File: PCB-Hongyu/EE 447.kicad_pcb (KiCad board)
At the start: 4 copper layers, 57.4 x 100 mm, 78 parts, among them J10 84952-4, J2 FH34SRJ-24S-0.5SH_99_, J3 S2B-PH-K-SLFSN, J4 Conn_01x01_Pin, J5 Conn_01x02_Pin, J6 Conn_01x01_Pin, J7 Conn_01x01_Pin, J8 Conn_01x02_Pin, J9 61302421121, Q1 BSS138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

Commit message: sdfghjk
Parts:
- Q2: footprint Package_TO_SOT_THT:TO-92_Inline -> Package_TO_SOT_SMD:SOT-23_Handsoldering
- moved Q2 2.80 mm to (206.5, 126.0)
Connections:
- J10 pad 5: GND -> (no net)
- J10 pad 6: GND -> (no net)
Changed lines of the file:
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@@
 			(psa4output no)
 			(plot_black_and_white yes)
+			(plotinvisibletext no)
 			(sketchpadsonfab no)
 			(plotpadnumbers no)
@@
 			)
 		)
-		(property "Datasheet" "https://www.digikey.com/en/products/detail/onsemi/BSS138/244210"
+		(property "Datasheet" "https://www.mouser.com/ProductDetail/onsemi-Fairchild/BSS138?qs=HK%252BeIG1iaahCeqBvjB4arg%3D%3D&srsltid=AfmBOoqSNHRxNY05tuDQ32Q_ya6yO_gO9lrnV_3A-Ol45sM-SCPd4I5t"
 			(at 0 0 0)
 			(layer "F.Fab")
@@
 			(size 2.667 3.6068)
 			(layers "F.Cu" "F.Mask" "F.Paste")
-			(net 1 "GND")
 		)
 		(pad "6" smd rect
@@
 			(size 2.667 3.6068)
 			(layers "F.Cu" "F.Mask" "F.Paste")
-			(net 1 "GND")
 		)
 		(embedded_fonts no)
@@
 		)
 	)
-	(footprint "Package_TO_SOT_THT:TO-92_Inline"
+	(footprint "Package_TO_SOT_SMD:SOT-23_Handsoldering"
 		(layer "F.Cu")
-		(at 209 127.27 90)
-		(descr "TO-92 leads in-line, narrow, oval pads, drill 0.75mm (see NXP sot054_po.pdf)")
-		(tags "to-92 sc-43 sc-43a sot54 PA33 transistor")
+		(at 206.5 126 90)
+		(descr "SOT-23, Handsoldering")
+		(tags "SOT-23")
 		(property "Reference" "Q2"
-			(at 1.27 -3.56 90)
+			(at 0 -2.75 90)
 			(layer "F.SilkS")
 			(effects
@@
 		)
 		(property "Value" "S8050"
-			(at 1.27 2.79 90)
+			(at 0 2.5 90)
 			(layer "F.Fab")
 			(effects
@@
 		(sheetname "/Epaper/")
 		(sheetfile "../PCB_June/PCB.kicad_sch")
-		(attr through_hole)
+		(attr smd)
 		(fp_line
-			(start -0.53 1.85)
-			(end 3.07 1.85)
+			(start 0.76 -1.58)
+			(end 0.76 -0.65)
 			(stroke
 				(width 0.12)
@@
 			(layer "F.SilkS")
 		)
-		(fp_arc
-			(start 1.27 -2.6)
-			(mid 3.672087 -0.994977)
-			(end 3.108478 1.838478)
+		(fp_line
+			(start -0.04 -1.58)
+			(end 0.76 -1.58)
 			(stroke
 				(width 0.12)
@@
 			(layer "F.SilkS")
 		)
-		(fp_arc
-			(start -0.568478 1.838478)
-			(mid -1.132087 -0.994977)
-			(end 1.27 -2.6)
+		(fp_line
+			(start -0.04 -1.58)
+			(end -0.84 -1.58)
+			(stroke
+				(width 0.12)
+				(type solid)
+			)
+			(layer "F.SilkS")
+		)
+		(fp_line
+			(start 0.76 1.58)
+			(end 0.76 0.65)
+			(stroke
+				(width 0.12)
+				(type solid)
+			)
+			(layer "F.SilkS")
+		)
+		(fp_line
+			(start 0.76 1.58)
+			(end -0.7 1.58)
 			(stroke
 				(width 0.12)
@@
 			(layer "F.SilkS")
 		)
+		(fp_poly
+			(pts
+				(xy -1.34 -1.61) (xy -1.58 -1.94) (xy -1.1 -1.94) (xy -1.34 -1.61)
+			)
+			(stroke
+				(width 0.12)
+				(type solid)
+			)
+			(fill yes)
+			(layer "F.SilkS")
+		)
 		(fp_line
-			(start -1.46 -2.73)
-			(end 4 -2.73)
+			(start 2.7 -1.75)
+			(end 2.7 1.75)
 			(stroke
 				(width 0.05)
@@
 		)
 		(fp_line
-			(start -1.46 -2.73)
-			(end -1.46 2.01)
+			(start -2.7 -1.75)
+			(end 2.7 -1.75)
 			(stroke
 				(width 0.05)
@@
 		)
 		(fp_line
-			(start 4 2.01)
-			(end 4 -2.73)
+			(start 2.7 1.75)
+			(end -2.7 1.75)
 			(stroke
 				(width 0.05)
@@
 		)
 		(fp_line
-			(start 4 2.01)
-			(end -1.46 2.01)
+			(start -2.7 1.75)
+			(end -2.7 -1.75)
 			(stroke
 				(width 0.05)
@@
 		)
 		(fp_line
-			(start -0.5 1.75)
-			(end 3 1.75)
+			(start 0.7 -1.52)
+			(end 0.7 1.52)
 			(stroke
 				(width 0.1)
@@
 			(layer "F.Fab")
 		)
-		(fp_arc
-			(start 1.27 -2.48)
-			(mid 3.561221 -0.949055)
-			(end 3.023625 1.753625)
+		(fp_line
+			(start -0.15 -1.52)
+			(end 0.7 -1.52)
 			(stroke
 				(width 0.1)
@@
 			(layer "F.Fab")
 		)
-		(fp_arc
-			(start -0.483625 1.753625)
-			(mid -1.021221 -0.949055)
-			(end 1.27 -2.48)
+		(fp_line
+			(start -0.7 -0.95)
+			(end -0.15 -1.52)
+			(stroke
+				(width 0.1)
+				(type solid)
+			)
+			(layer "F.Fab")
+		)
+		(fp_line
+			(start -0.7 -0.95)
+			(end -0.7 1.5)
+			(stroke
+				(width 0.1)
+				(type solid)
+			)
+			(layer "F.Fab")
+		)
+		(fp_line
+			(start -0.7 1.52)
+			(end 0.7 1.52)
 			(stroke
 				(width 0.1)
@@
 		)
 		(fp_text user "${REFERENCE}"
-			(at 1.27 0 90)
+			(at 0 0 180)
 			(layer "F.Fab")
 			(effects
 				(font
-					(size 1 1)
-					(thickness 0.15)
+					(size 0.5 0.5)
+					(thickness 0.075)
 				)
 			)
 		)
-		(pad "1" thru_hole rect
-			(at 0 0 90)
-			(size 1.05 1.5)
-			(drill 0.75)
-			(layers "*.Cu" "*.Mask")
-			(remove_unused_layers no)
+		(pad "1" smd roundrect
+			(at -1.5 -0.95 90)
+			(size 1.9 0.8)
+			(layers "F.Cu" "F.Mask" "F.Paste")
+			(roundrect_rratio 0.25)
 			(net 1 "GND")
 			(pinfunction "E")
 			(pintype "passive")
 		)
-		(pad "2" thru_hole oval
-			(at 1.27 0 90)
-			(size 1.05 1.5)
-			(drill 0.75)
-			(layers "*.Cu" "*.Mask")
-			(remove_unused_layers no)
+		(pad "2" smd roundrect
+			(at -1.5 0.95 90)
+			(size 1.9 0.8)
+			(layers "F.Cu" "F.Mask" "F.Paste")
+			(roundrect_rratio 0.25)
 			(net 13 "Net-(Q2-B)")
 			(pinfunction "B")
 			(pintype "input")
 		)
-		(pad "3" thru_hole oval
-			(at 2.54 0 90)
-			(size 1.05 1.5)
-			(drill 0.75)
-			(layers "*.Cu" "*.Mask")
-			(remove_unused_layers no)
+		(pad "3" smd roundrect
+			(at 1.5 0 90)
+			(size 1.9 0.8)
+			(layers "F.Cu" "F.Mask" "F.Paste")
+			(roundrect_rratio 0.25)
 			(net 12 "Net-(Q2-C)")
 			(pinfunction "C")
@@
 		)
 		(embedded_fonts no)
-		(model "${KICAD9_3DMODEL_DIR}/Package_TO_SOT_THT.3dshapes/TO-92_Inline.wrl"
+		(model "${KICAD9_3DMODEL_DIR}/Package_TO_SOT_SMD.3dshapes/SOT-23.wrl"
 			(offset
 				(xyz 0 0 0)

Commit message: bjt
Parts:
- Q2: value S8050 -> SMD-TRANSISTORS-NPN-25V-500MW_SOT-23_; footprint Package_TO_SOT_SMD:SOT-23_Handsoldering -> Library:S8050_SOT-23
- moved Q2 55.5 mm to (261.9, 129.1), turned to 0 degrees
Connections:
- Q2 pad 1: GND -> Net-(Q2-Pad1)
- Q2 pad 2: Net-(Q2-B) -> GND
- R4 pad 1: Net-(Q2-B) -> Net-(Q2-Pad1)
- R6 pad 2: Net-(Q2-B) -> Net-(Q2-Pad1)
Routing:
- net Net-(Q2-Pad1): track 0.00 -> 7.68 mm
- net Net-(Q2-B): track 7.68 -> 0.00 mm

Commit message: i think i changed it good maybe
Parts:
- moved Q2 52.5 mm to (209.5, 127.0), turned to 90 degrees
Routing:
- net Net-(Q2-Pad1): track 7.68 -> 5.74 mm
- net Net-(Q2-Pad3): track 7.32 -> 8.03 mm
- net GND: track 204.3 -> 203.8 mm, vias 446 -> 447
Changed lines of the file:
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@@
 			(psa4output no)
 			(plot_black_and_white yes)
+			(plotinvisibletext no)
 			(sketchpadsonfab no)
 			(plotpadnumbers no)
@@
 	(footprint "Library:S8050_SOT-23"
 		(layer "F.Cu")
-		(at 261.911 129.084)
+		(at 209.5 127 90)
 		(descr "<b>SOT23</b>")
 		(property "Reference" "Q2"
-			(at 0.317628 -2.350438 0)
+			(at 0.317628 -2.350438 90)
 			(layer "F.SilkS")
 			(effects
@@
 		)
 		(property "Value" "SMD-TRANSISTORS-NPN-25V-500MW_SOT-23_"
-			(at 0.635323 2.47775 0)
+			(at 0.635323 2.47775 90)
 			(layer "F.Fab")
 			(effects
@@
 		)
 		(property "Datasheet" ""
-			(at 0 0 0)
+			(at 0 0 90)
 			(layer "F.Fab")
 			(hide yes)
@@
 		)
 		(property "Description" ""
-			(at 0 0 0)
+			(at 0 0 90)
 			(layer "F.Fab")
 			(hide yes)
@@
 		)
 		(property "MF" "UMW"
-			(at 0 0 0)
+			(at 0 0 90)
 			(unlocked yes)
 			(layer "F.Fab")
@@
 		)
 		(property "Description_1" "Bipolar (BJT) Transistor NPN 25 V 500 mA 150MHz 300 mW Surface Mount SOT-23"
-			(at 0 0 0)
+			(at 0 0 90)
 			(unlocked yes)
 			(layer "F.Fab")
@@
 		)
 		(property "Package" "None"
-			(at 0 0 0)
+			(at 0 0 90)
 			(unlocked yes)
 			(layer "F.Fab")
@@
 		)
 		(property "MPN" "S8050"
-			(at 0 0 0)
+			(at 0 0 90)
 			(unlocked yes)
 			(layer "F.Fab")
@@
 		)
 		(property "Price" "None"
-			(at 0 0 0)
+			(at 0 0 90)
 			(unlocked yes)
 			(layer "F.Fab")
@@
 		)
 		(property "SnapEDA_Link" "https://www.snapeda.com/parts/S8050/UMW/view-part/?ref=snap"
-			(at 0 0 0)
+			(at 0 0 90)
 			(unlocked yes)
 			(layer "F.Fab")
@@
 		)
 		(property "MP" "S8050"
-			(at 0 0 0)
+			(at 0 0 90)
 			(unlocked yes)
 			(layer "F.Fab")
@@
 		)
 		(property "Availability" "In Stock"
-			(at 0 0 0)
+			(at 0 0 90)
 			(unlocked yes)
 			(layer "F.Fab")
@@
 		)
 		(property "Check_prices" "https://www.snapeda.com/parts/S8050/UMW/view-part/?ref=eda"
-			(at 0 0 0)
+			(at 0 0 90)
 			(unlocked yes)
 			(layer "F.Fab")
@@
 		(attr smd)
 		(fp_line
-			(start -1.4605 -0.635)
-			(end -1.4605 0.254)
+			(start 1.4605 -0.635)
+			(end 0.6985 -0.635)
 			(stroke
 				(width 0.127)
@@
 		)
 		(fp_line
-			(start 1.4605 -0.635)
-			(end 0.6985 -0.635)
+			(start -1.4605 -0.635)
+			(end -1.4605 0.254)
 			(stroke
 				(width 0.127)
@@
 		(fp_poly
 			(pts
-				(xy -1.16846 0.7112) (xy -0.7112 0.7112) (xy -0.7112 1.29547) (xy -1.16846 1.29547)
+				(xy -0.228612 -1.2954) (xy 0.2286 -1.2954) (xy 0.2286 -0.711238) (xy -0.228612 -0.711238)
 			)
 			(stroke
@@
 		(fp_poly
 			(pts
-				(xy -0.228612 -1.2954) (xy 0.2286 -1.2954) (xy 0.2286 -0.711238) (xy -0.228612 -0.711238)
+				(xy 0.711335 0.7112) (xy 1.1684 0.7112) (xy 1.1684 1.29565) (xy 0.711335 1.29565)
 			)
 			(stroke
@@
 		(fp_poly
 			(pts
-				(xy 0.711335 0.7112) (xy 1.1684 0.7112) (xy 1.1684 1.29565) (xy 0.711335 1.29565)
+				(xy -1.16846 0.7112) (xy -0.7112 0.7112) (xy -0.7112 1.29547) (xy -1.16846 1.29547)
 			)
 			(stroke
@@
 		)
 		(pad "1" smd rect
-			(at -0.889 1.016)
+			(at -0.889 1.016 90)
 			(size 1.016 1.143)
 			(layers "F.Cu" "F.Mask" "F.Paste")
@@
 		)
 		(pad "2" smd rect
-			(at 0.889 1.016)
+			(at 0.889 1.016 90)
 			(size 1.016 1.143)
 			(layers "F.Cu" "F.Mask" "F.Paste")
@@
 		)
 		(pad "3" smd rect
-			(at 0 -1.016)
+			(at 0 -1.016 90)
 			(size 1.016 1.143)
 			(layers "F.Cu" "F.Mask" "F.Paste")
@@
 	)
 	(segment
-		(start 209.09 127)
-		(end 209 127)
-		(width 0.3)
-		(layer "F.Cu")
-		(net 1)
-	)
-	(segment
 		(start 189 174.2)
 		(end 189 173.0375)
@@
 	)
 	(segment
-		(start 209.09 127)
-		(end 209.36 127.27)
-		(width 0.3)
-		(layer "F.Cu")
-		(net 1)
-	)
-	(segment
 		(start 223.54 145.96)
 		(end 223.5 146)
@@
 	)
 	(via
+		(at 210.516 126.111)
+		(size 0.6)
+		(drill 0.3)
+		(layers "F.Cu" "B.Cu")
+		(net 1)
+	)
+	(via
 		(at 193.5 113)
 		(size 0.6)
@@
 	)
 	(segment
-		(start 214 124.1)
-		(end 209.99 124.1)
-		(width 0.3)
+		(start 213 127)
+		(end 208.484 127)
+		(width 0.2)
 		(layer "F.Cu")
 		(net 12)
 	)
 	(segment
-		(start 213.95 124.15)
-		(end 214 124.1)
-		(width 0.3)
+		(start 213.5 124.325)
+		(end 213.95 123.875)
+		(width 0.2)
 		(layer "F.Cu")
 		(net 12)
 	)
 	(segment
-		(start 209.99 124.1)
-		(end 209.36 124.73)
-		(width 0.3)
+		(start 213.5 126.5)
+		(end 213 127)
+		(width 0.2)
 		(layer "F.Cu")
 		(net 12)
 	)
 	(segment
-		(start 213.95 126.5)
-		(end 213.95 124.15)
-		(width 0.3)
+		(start 213.5 126.5)
+		(end 213.5 124.325)
+		(width 0.2)
 		(layer "F.Cu")
 		(net 12)
 	)
 	(segment
-		(start 211 126)
-		(end 213.5 128.5)
-		(width 0.3)
+		(start 211.127 128.5)
+		(end 210.516 127.889)
+		(width 0.2)
 		(layer "F.Cu")
 		(net 13)
 	)
 	(segment
-		(start 209.36 126)
-		(end 211 126)
+		(start 213.5 131)
+		(end 213.5 128.5)
 		(width 0.3)
 		(layer "F.Cu")
@@
 	)
 	(segment
-		(start 213.5 131)
-		(end 213.5 128.5)
-		(width 0.3)
+		(start 213.5 128.5)
+		(end 211.127 128.5)
+		(width 0.2)
 		(layer "F.Cu")
 		(net 13)

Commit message: silkscreen
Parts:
- moved G*** 17.3 mm to (214.2, 187.2)
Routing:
- net CS_TSC: track 87.0 -> 87.6 mm
- net GND: vias 447 -> 454
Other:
- board text added: "GND"
- board text added: "June Shao, Claire Yuan, Hongyu Zhao"
- board text added: "SMART PAPER"
- board text added: "power circuitry"

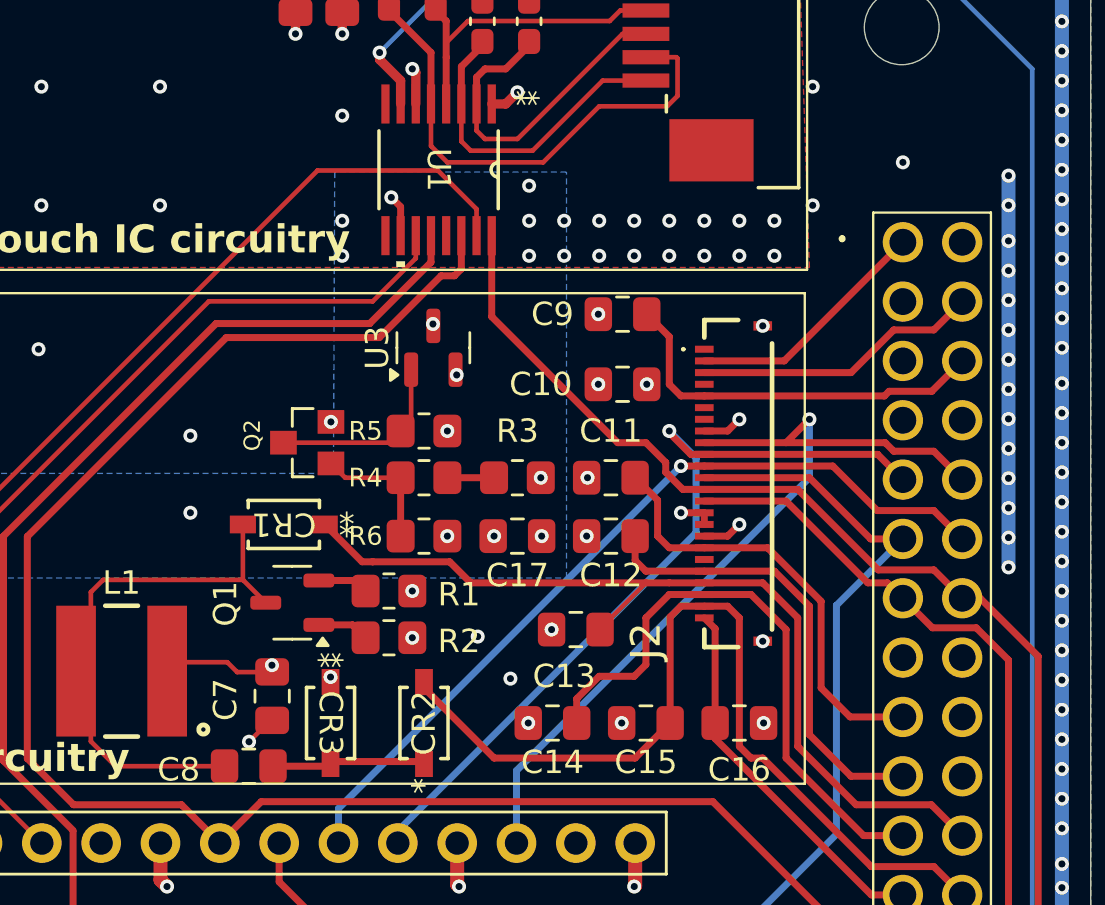
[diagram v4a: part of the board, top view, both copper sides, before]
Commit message: checked DRC but check again ig, i checked all my footprint
 i made a small change connecting 15 and 16
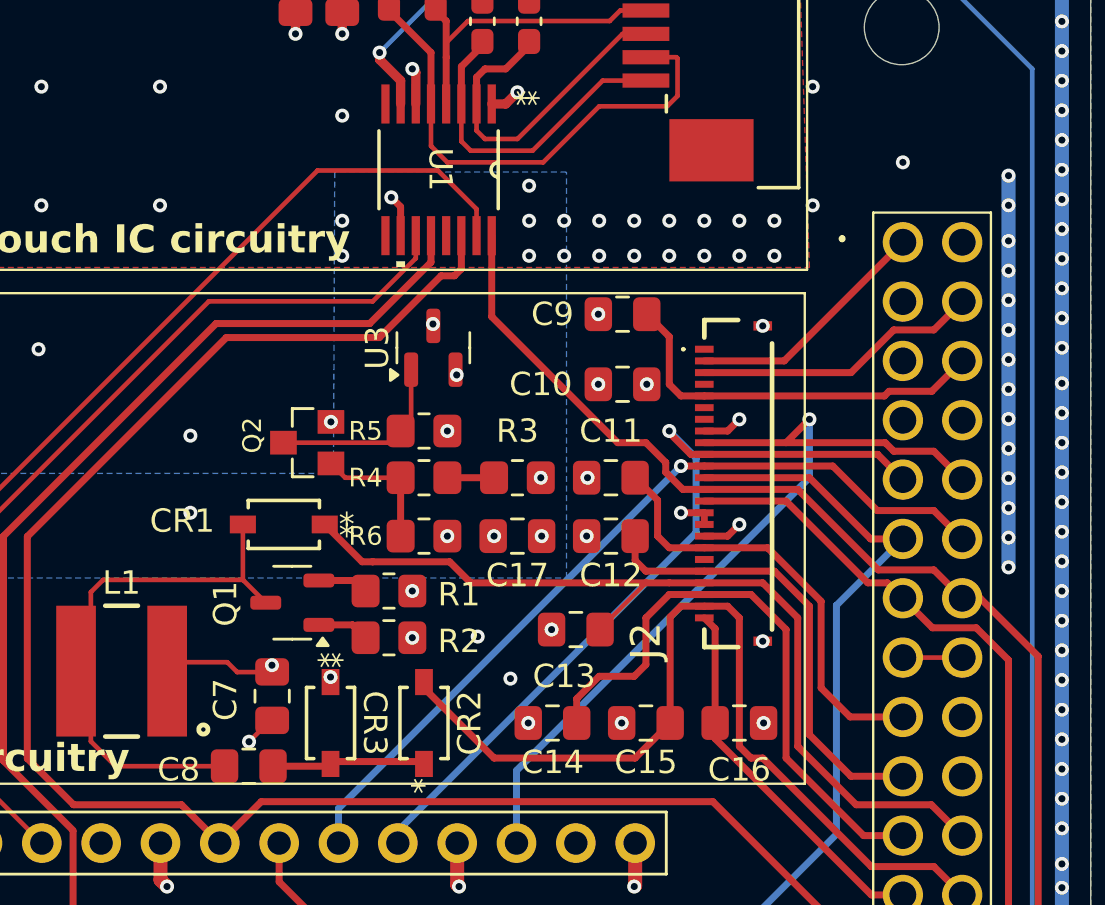
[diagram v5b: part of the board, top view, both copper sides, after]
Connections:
- J9 pad 15: unconnected-(J9-Pad15) -> /Epaper/3V3_OUT
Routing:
- net /Epaper/3V3_OUT: track 29.2 -> 31.9 mm

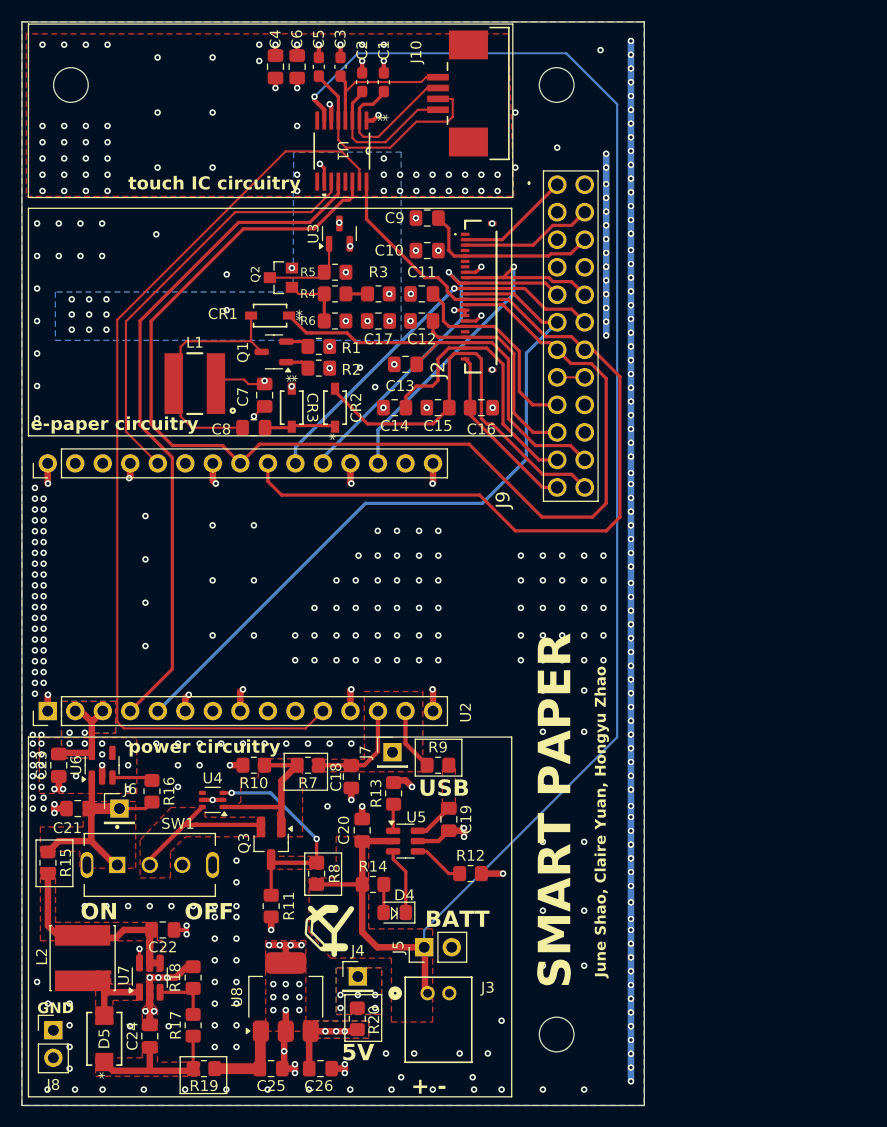
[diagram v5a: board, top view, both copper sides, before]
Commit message: penirq change pin
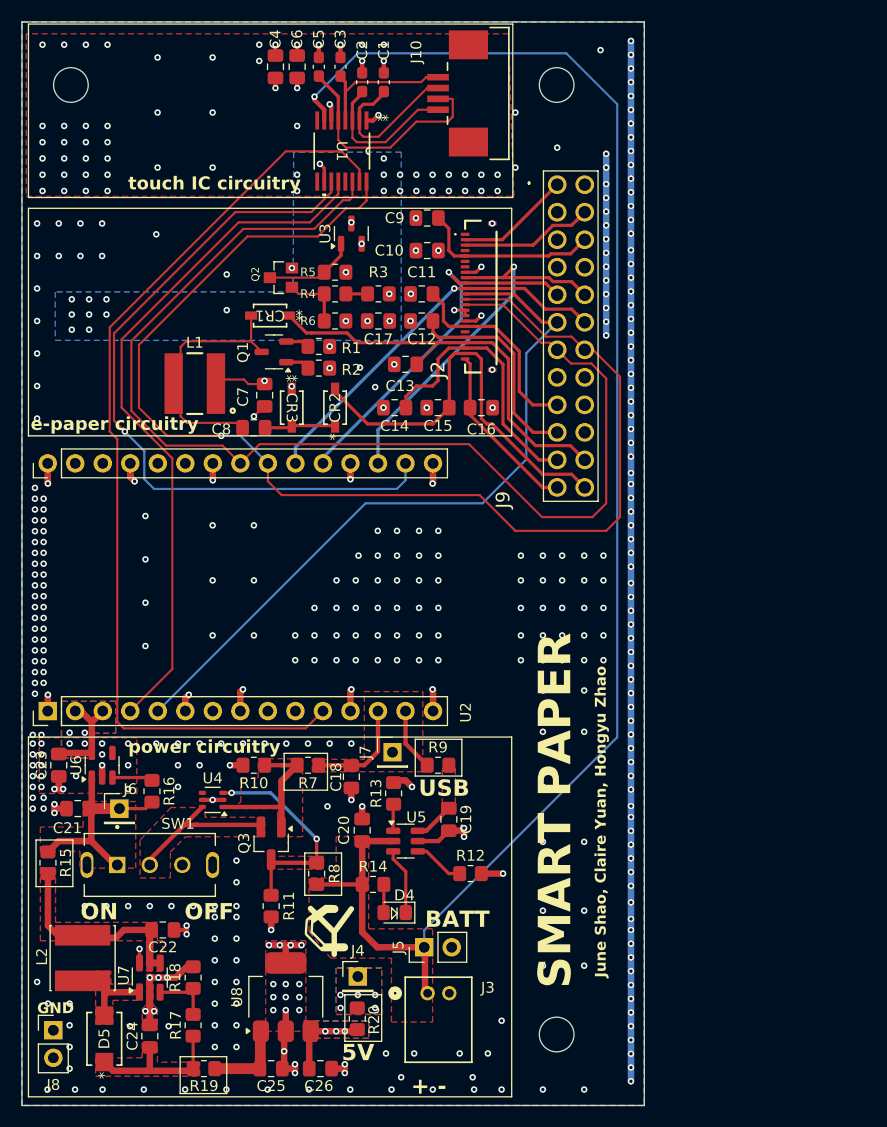
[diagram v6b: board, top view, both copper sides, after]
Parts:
- moved U3 1.10 mm to (216.0, 122.9)
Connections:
- U2 pad 20: /PENIRQ -> unconnected-(U2-IO9-Pad20)
- U2 pad 29: unconnected-(U2-IO19-Pad29) -> /PENIRQ
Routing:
- net CLK: track 83.3 -> 115.3 mm, vias 0 -> 1
- net /PENIRQ: track 39.2 -> 67.4 mm, vias 0 -> 1
- net MOSI: track 109.2 -> 111.0 mm
- net /Epaper/3V3_OUT: track 31.9 -> 30.3 mm
- net MISO: track 63.1 -> 64.5 mm
- net Net-(Q2-Pad3): track 8.03 -> 9.13 mm
- net unconnected-(U2-IO9-Pad20): track 0.00 -> 0.60 mm
- net CS_TSC: track 87.6 -> 88.2 mm
- net +3.3V: vias 18 -> 17
